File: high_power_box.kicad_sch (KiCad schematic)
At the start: 25 parts, among them K10 SPST-NO, 24V, 30A, K5 SPST-NO, 24V, 30A, K6 DCNLEV100, K7 DCNLEV100, K8 DCNLEV100, K9 SPST-NO, 24V, 50A, SW6 SW_Push

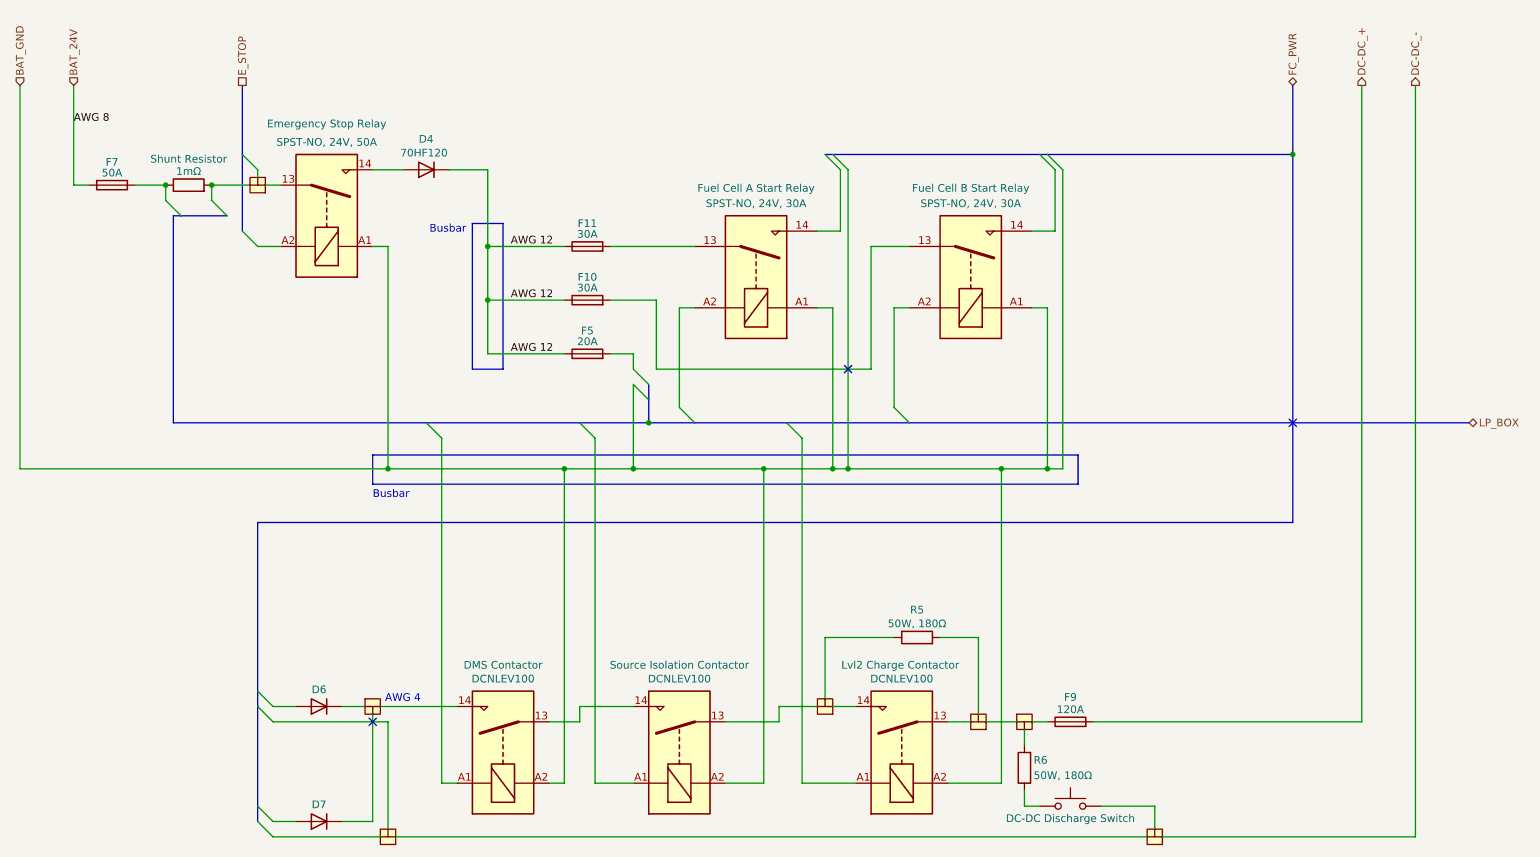
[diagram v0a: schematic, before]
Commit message: Move Dashboard to its own page
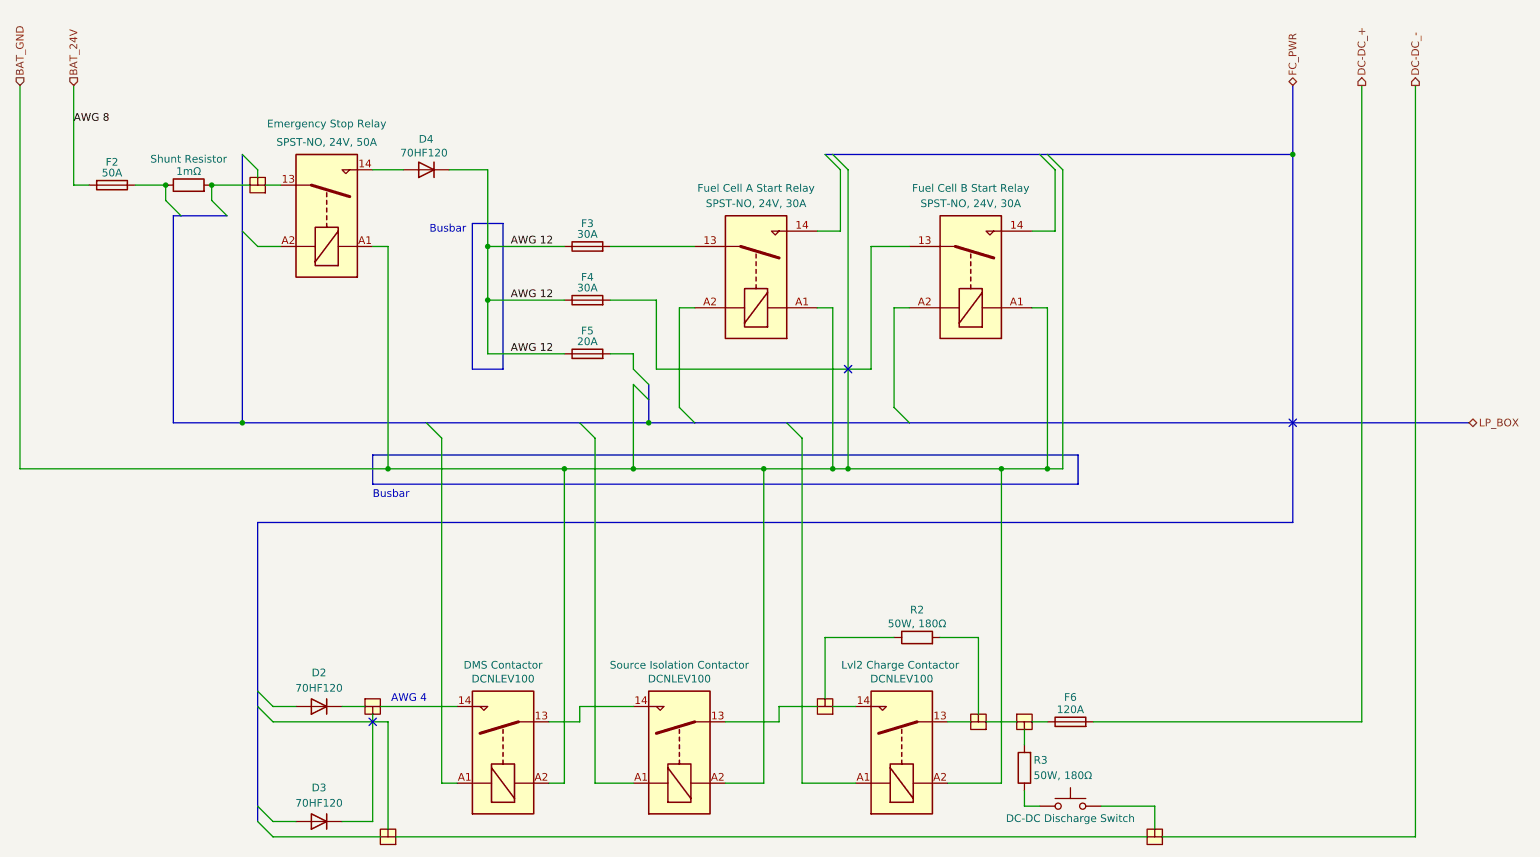
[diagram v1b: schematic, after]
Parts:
- renumbered C14 to C1, C9 to C2, C10 to C3, C11 to C4, C12 to C5, C13 to C6, C15 to C7, D6 to D2, D7 to D3, F7 to F2, F11 to F3, F10 to F4, F9 to F6, K9 to K1, K6 to K2, K7 to K3, K5 to K4, K8 to K5, K10 to K6, R4 to R1, R5 to R2, R6 to R3, SW6 to SW5
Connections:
- net at C3.: no longer C7.
- net at C1.: now also K1.13
- new net: C3., C7.
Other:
- company: Exocet -> Exocet Polytechnique Montréal

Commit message: Start low power box sheet
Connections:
- net at C3.: no longer C7.
- net at C1.: now also K1.13
- new net: C3., C7.
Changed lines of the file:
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@@
 	)
 	(symbol
-		(lib_name "Exocet_Electrical:Connector_3")
 		(lib_id "Exocet_Electrical:Connector_3")
 		(at 63.5 49.53 180)

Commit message: Complete Low Power Box
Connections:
- net at C3.: no longer C7.
- net at C1.: now also K1.13
- new net: C3., C7.
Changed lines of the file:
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@@
 	(title_block
 		(title "High Power Box Layout")
-		(date "2024-05-16")
-		(rev "1.1.1")
+		(date "2024-05-19")
+		(rev "1.2.0")
 		(company "Exocet Polytechnique Montréal")
 	)
@@
 	)
 	(rectangle
-		(start 82.55 91.694)
-		(end 199.39 96.52)
+		(start 83.185 92.075)
+		(end 198.755 95.885)
 		(stroke
 			(width 0)
@@
 	(text "Busbar"
 		(exclude_from_sim no)
-		(at 85.598 98.298 0)
+		(at 85.598 97.536 0)
 		(effects
 			(font

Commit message: Finalize layout
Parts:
- removed R1: 1mΩ, symbol Device:R
- added BSEN1: ~, symbol Exocet_Electrical:Battery_Sense
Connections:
- net at C3.: no longer C7.
- net at F2.1: now also BSEN1. (~{ALCC})
- net at C1.: now also K1.13
- new net: C3., C7.
- new net: BSEN1. (~{ALCC}), C1.

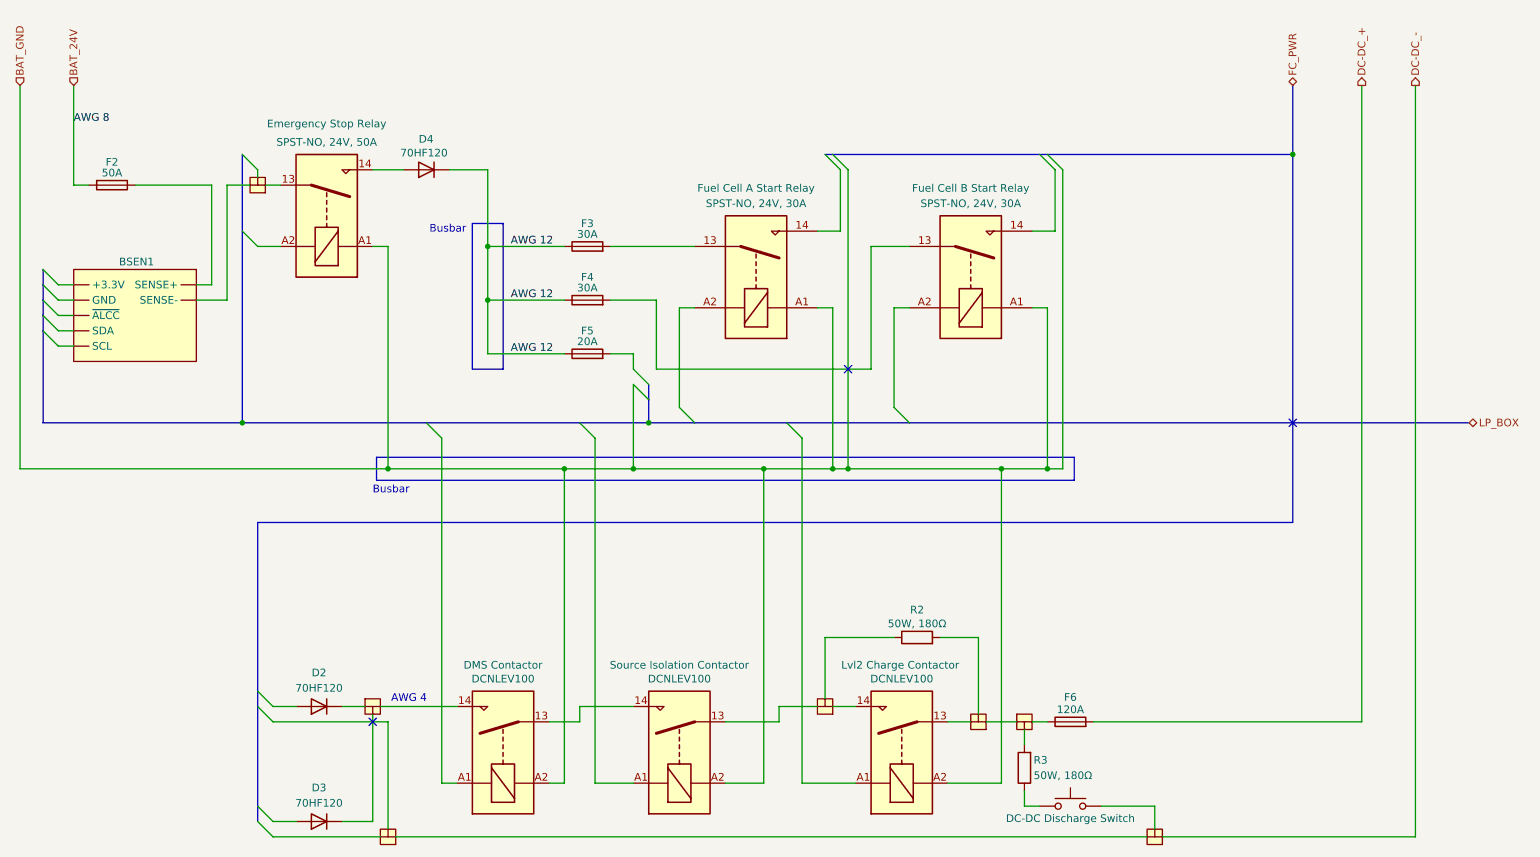
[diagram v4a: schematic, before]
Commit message: Add labels
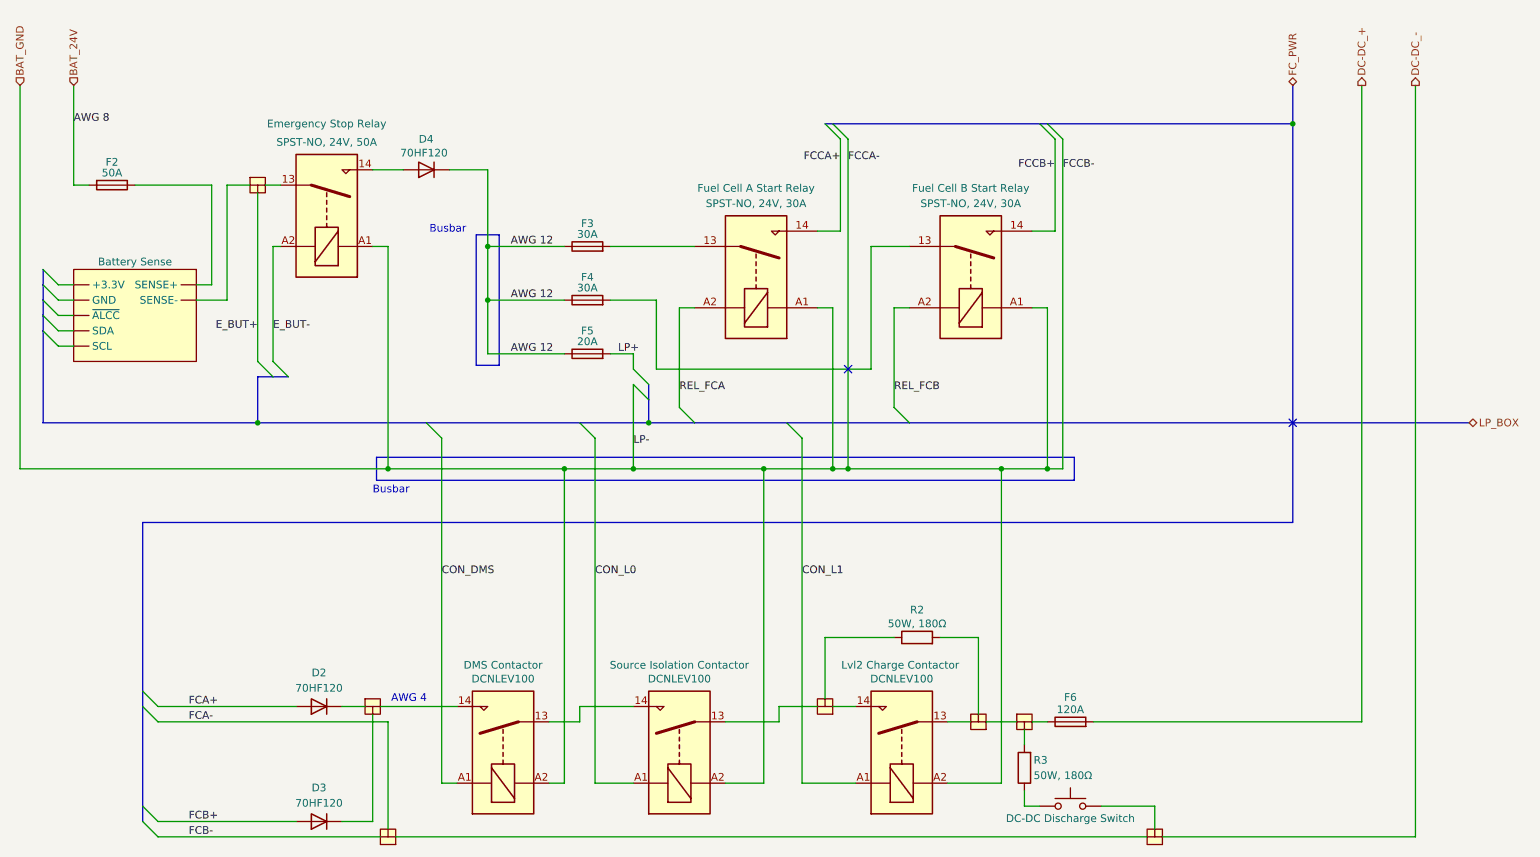
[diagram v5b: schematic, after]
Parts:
- BSEN1: Name (none) -> Battery Sense
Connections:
- net FCB-: now reaches C3.
- net FCB-: no longer C7.
- net CON_L1: now reaches K5.A1
- net CON_L0: now reaches K3.A1
- net CON_DMS: now reaches K2.A1
- net FCB+: now reaches D3.2 (A)
- net E_BUT+: now reaches C1.
- net at BSEN1. (~{ALCC}): now also F2.1; no longer C1.
- net LP+: now reaches F5.2
- net FCCA+: now reaches K4.14
- net REL_FCA: now reaches K4.A2
- net FCA+: now reaches D2.2 (A)
- net FCCB+: now reaches K6.14
- net REL_FCB: now reaches K6.A2
- net E_BUT-: now reaches K1.A2
- new net: C3., C7.
- new net: BSEN1. (~{ALCC}), C1.
- new net FCA-: C3.
- no-connect marks 3 -> 2
